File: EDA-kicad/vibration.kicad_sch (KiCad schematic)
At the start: 4 parts

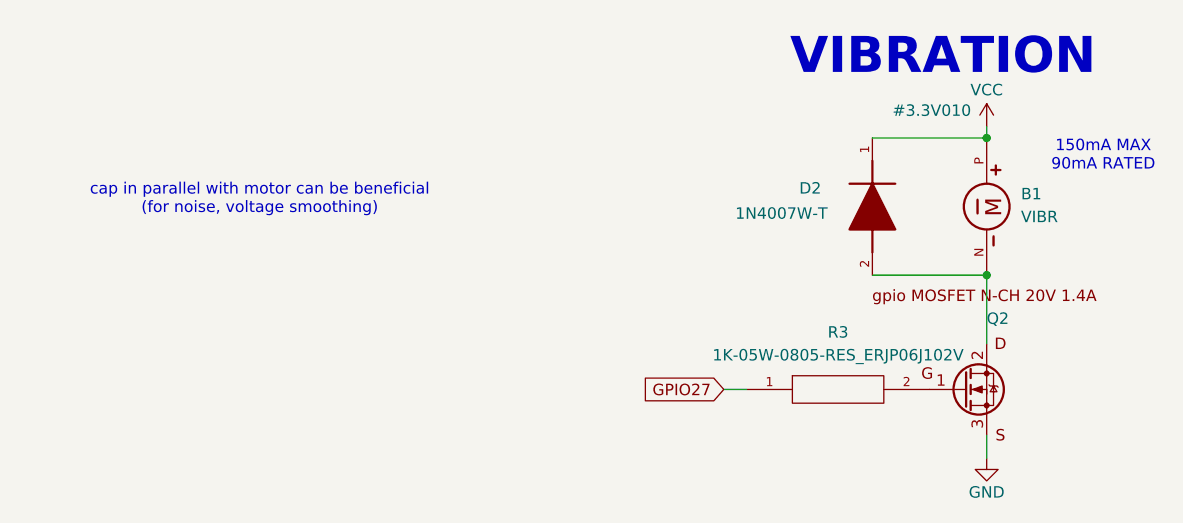
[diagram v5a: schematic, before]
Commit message: reannotate entire schematic
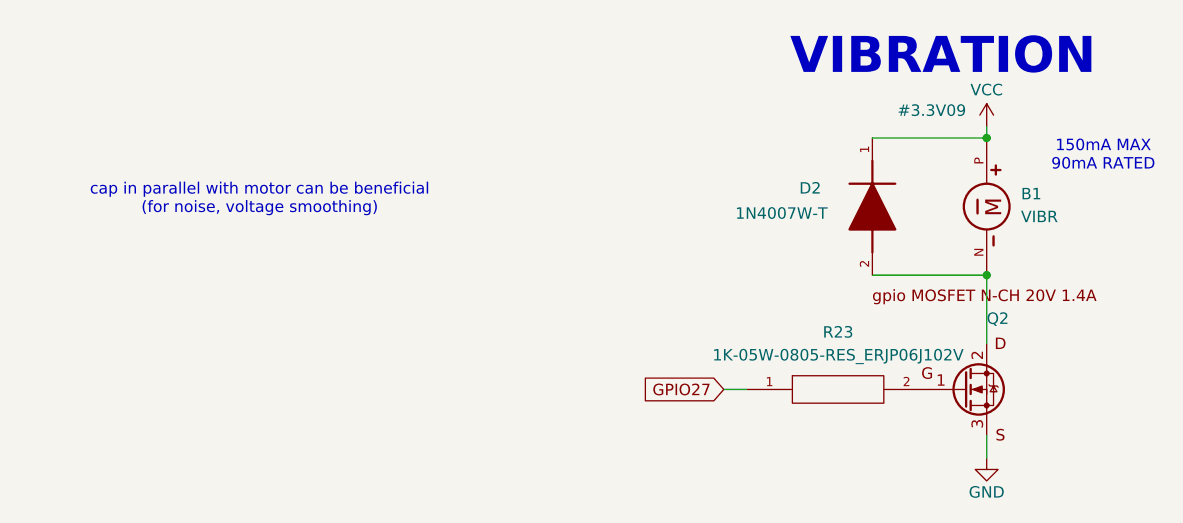
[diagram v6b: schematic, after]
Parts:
- renumbered R3 to R23
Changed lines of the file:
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@@
 			"AAAAAAAAAAAAAAAAAAAAAAAAAAAAAAAAAAAAAAAAAAAAAAAAAAAAAAAAAAAAAAAAAAAAAAAAAAAA"
 			"AAAAAAAAAAAAAAAAAAAAAAAAAAAAAAAAAAAAAAAAAAAAAAAAAAAAAAAAAAAAAAAAAAAAAAAAAAAA"
-			"AAAAAAAAAAAAAAAAAAAAAAAAAAAAAAAAAAAAAAAAAAAAAAAAAAAAAAAAAAAAAAAAAA=="
+			"AAAAAAAAAAAAAAAAAAAAAAAAAAAAAAAAAAAAAAAAAAAAAAAAAAAAAAAAAAAAAAAAAFUAABgAAAAA"
+			"AAAAGAAAAAAAAAAeAAAAAAAAAMDF6qdVVQAAGQAAAAAAAAAZAAAAAAAAAEhEU1AtNzUwkPkFJVZV"
+			"AAATAAAAAAAAABMAAAAAAAAAAAAAAAAAAACw2F6eVVUAABEAAAAAAAAAEQAAAAAAAAAwAAAAAAAA"
+			"AHAT8ilWVQAADgAAAAAAAABUZVggR3lyZSBCb251bQAAQHl3wVVVAAATAAAAAAAAABMAAAAAAAAA"
+			"gBfyKVZVAACwE/IpVlUAAA8AAAAAAAAAVGVYIEd5cmUgQ2hvcnVzANAT8ilWVQAADwAAAAAAAABU"
+			"ZVggR3lyZSBDdXJzb3IAoHYIJVZVAAAUAAAAAAAAABQAAAAAAAAA8BXyKVZVAAAQFPIpVlUAAA4A"
+			"AAAAAAAAVGVYIEd5cmUgSGVyb3MAAIAsMsFVVQAAEQAAAAAAAAARAAAAAAAAAAAAAAAAAAAAUNK3"
+			"81VVAAAQAAAAAAAAABAAAAAAAAAAAAAAAAAAAABgmJynVVUAABUAAAAAAAAAFQAAAAAAAACRAAAA"
+			"AAAAAJAU8ilWVQAADwAAAAAAAABUZVggR3lyZSBTY2hvbGEA8FxhwVVVAAAUAAAAAAAAABQAAAAA"
+			"AAAAAAAAAAAAAADQFPIpVlUAAA8AAAAAAAAAVGVYIEd5cmUgVGVybWVzAICUGRNWVQAAFAAAAAAA"
+			"AAAUAAAAAAAAAAAAAAAAAAAAEA8B1VVVAAATAAAAAAAAABMAAAAAAAAAUwAAAFAAAABAC5GpVVUA"
+			"ABgAAAAAAAAAGAAAAAAAAACRAAAAAAAAAJBq8CVWVQAAGQAAAAAAAAAZAAAAAAAAAAAAAAAAAAAA"
+			"cBXyKVZVAAAFAAAAAAAAAFRpbm9zAAAAAAAAAAAAAACQFfIpVlUAAAsAAAAAAAAAVVJXIEJvb2tt"
+			"YW4AAAAAALAV8ilWVQAACgAAAAAAAABVUlcgR290aGljAAAAAAAAIEqtrFVVAAATAAAAAAAAABMA"
+			"AAAAAAAAQ2hhcmFjdGWwRSaoVVUAABgAAAAAAAAAGAAAAAAAAABRAQAAAAAAACDtd/JVVQAAGAAA"
+			"AAAAAAAYAAAAAAAAAMAW8ilWVQAAMBbyKVZVAAAGAAAAAAAAAFV0b3BpYQAAMEBb9Bh/AABQFvIp"
+			"VlUAAAQAAAAAAAAAWjAwMwBVAAABAAAAAAAAAHAW8ilWVQAABgAAAAAAAABjbWV4MTAAAAAAAAAA"
+			"AAAAkBbyKVZVAAAGAAAAAAAAAGNtbWkxMAAAUwAAAFAAAACwFvIpVlUAAAUAAAAAAAAAY21yMTAA"
+			"AACRAAAAAAAAANAW8ilWVQAABgAAAAAAAABjbXN5MTAAAAAAAAAAAAAA8BbyKVZVAA=="
 		)
 	)
@@
 		(on_board yes)
 		(dnp no)
-		(property "Reference" "#PWR03"
+		(property "Reference" "#PWR0129"
 			(at 176.53 124.46 0)
 			(effects
@@
 			(project "cm5-carrier"
 				(path "/28c5e4fe-1ec7-4477-97f0-d2ec1401fad5/b44a98f4-0347-4633-8437-b3dfeaa625db"
-					(reference "#PWR03")
+					(reference "#PWR0129")
 					(unit 1)
 				)
@@
 		(dnp no)
 		(fields_autoplaced yes)
-		(property "Reference" "R3"
+		(property "Reference" "R23"
 			(at 160.02 104.14 0)
 			(effects
@@
 			(project "cm5-carrier"
 				(path "/28c5e4fe-1ec7-4477-97f0-d2ec1401fad5/b44a98f4-0347-4633-8437-b3dfeaa625db"
-					(reference "R3")
+					(reference "R23")
 					(unit 1)
 				)
@@
 		(on_board yes)
 		(dnp no)
-		(property "Reference" "#3.3V010"
+		(property "Reference" "#3.3V09"
 			(at 170.434 79.502 0)
 			(effects
@@
 			(project "cm5-carrier"
 				(path "/28c5e4fe-1ec7-4477-97f0-d2ec1401fad5/b44a98f4-0347-4633-8437-b3dfeaa625db"
-					(reference "#3.3V010")
+					(reference "#3.3V09")
 					(unit 1)
 				)

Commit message: add new switches and reannotate
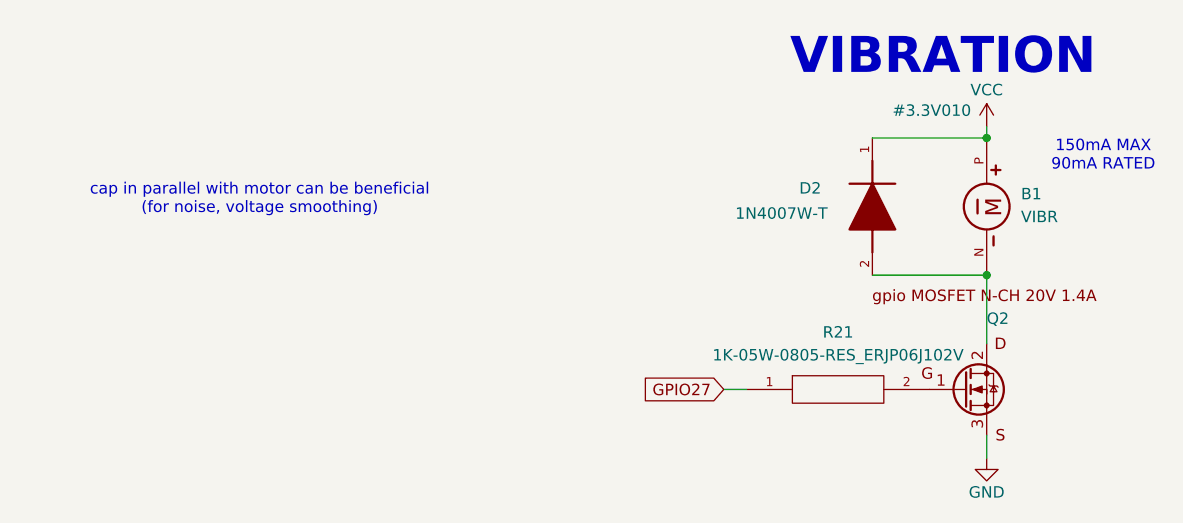
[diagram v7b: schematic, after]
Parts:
- renumbered R23 to R21

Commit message: POWER SCHEMATIC FINISHED
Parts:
- Q3: renamed from Q2; MPN (none) -> BSS816NWH6327XTSA1
- renumbered R21 to R24
